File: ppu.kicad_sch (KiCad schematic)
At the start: 17 parts, among them U1 STM32U073CCUx, Y4 CM7V-T1A-32.768KHZ

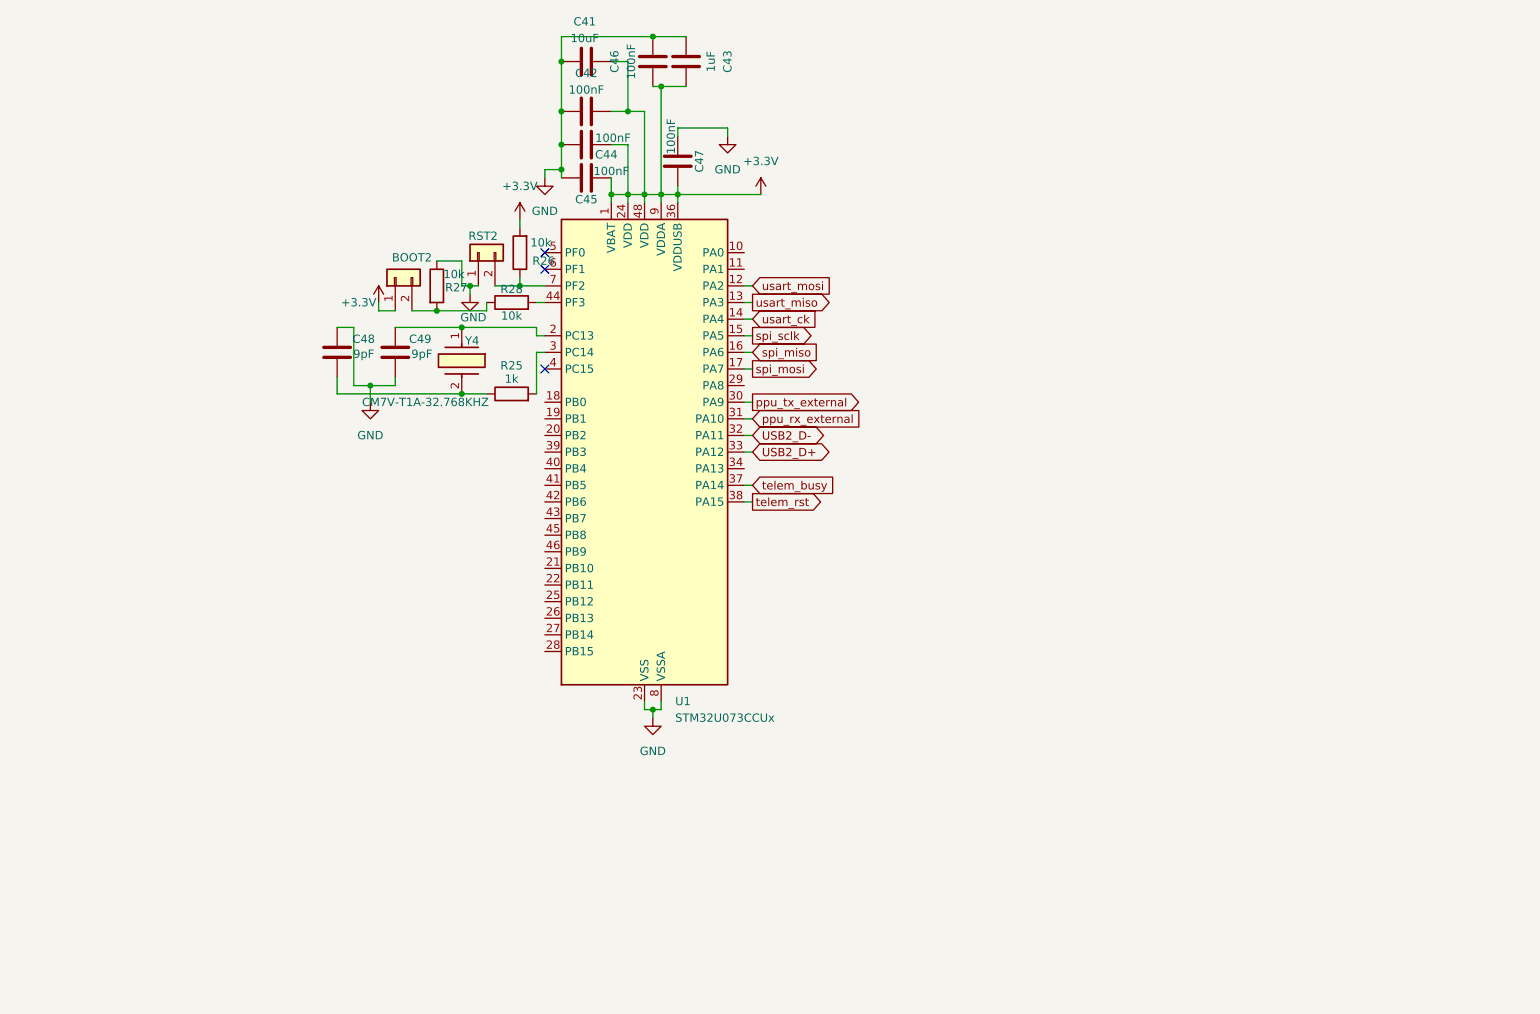
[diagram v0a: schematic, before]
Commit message: added in the flash chip and micro sd card, rerouted some stuff, looking real nice rn - still need to finish rf, pyros, and add in the piezo
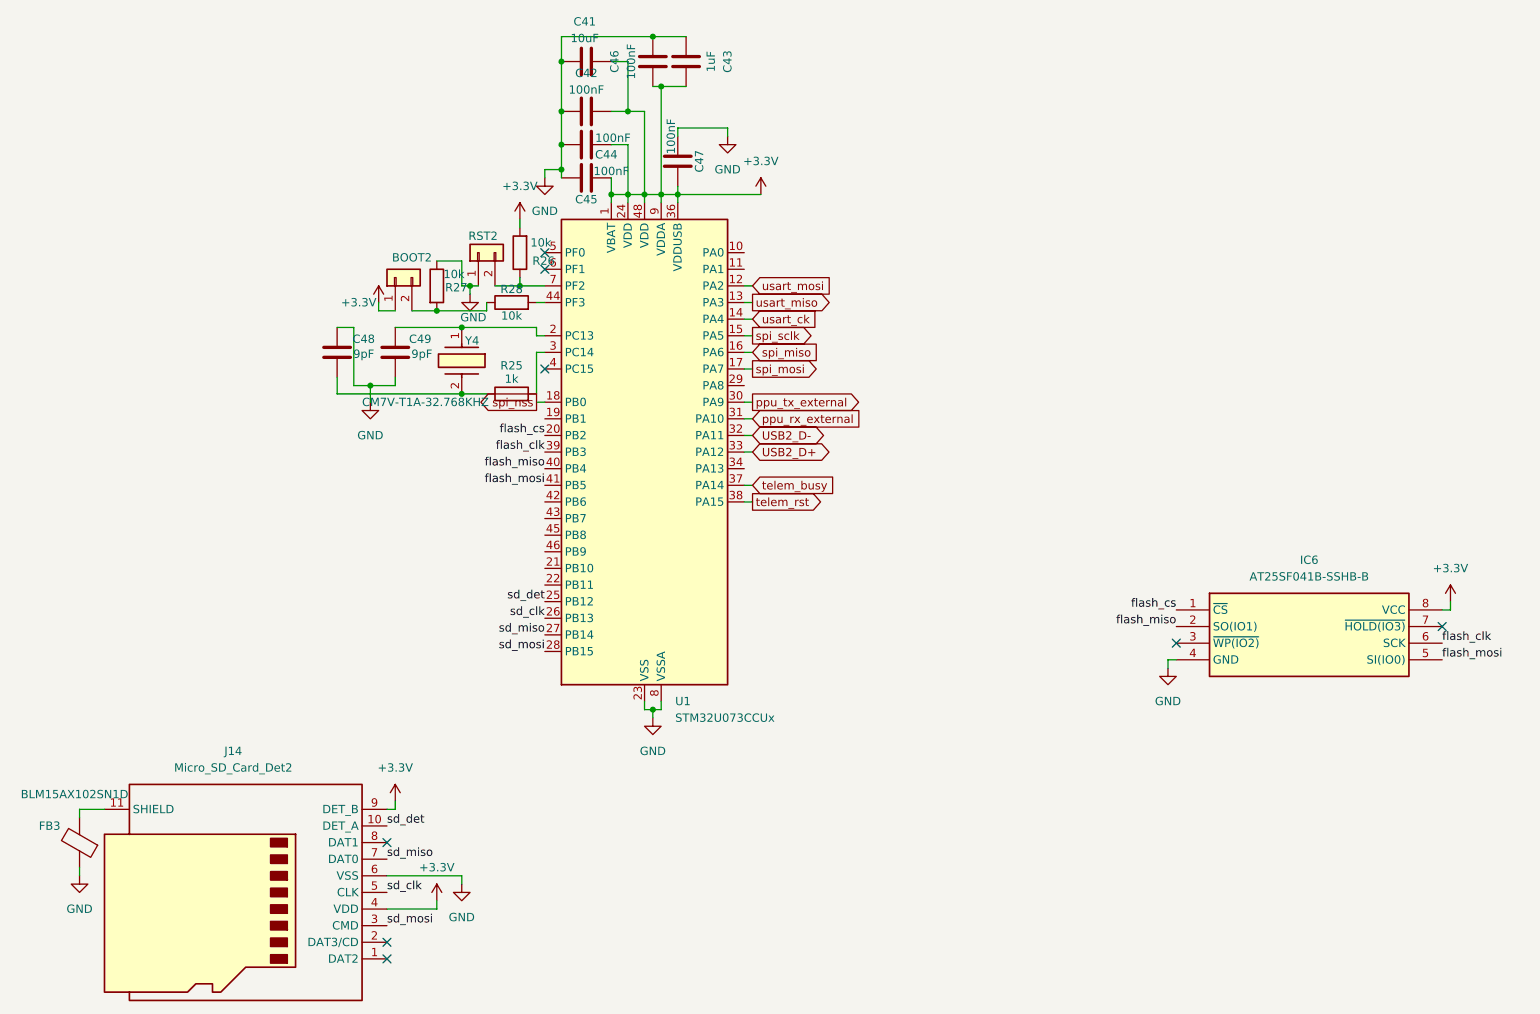
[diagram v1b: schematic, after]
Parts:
- added FB3: BLM15AX102SN1D, footprints:NFZ15SG152SN10B, symbol Device:FerriteBead
- added IC6: AT25SF041B-SSHB-B, footprints:SOIC127P600X175-8N, symbol AT25SF041B-SSHB-B:AT25SF041B-SSHB-B
- added J14: Micro_SD_Card_Det2, Connector_Card:microSD_HC_Molex_104031-0811, symbol Connector:Micro_SD_Card_Det2
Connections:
- net +3.3V: now also IC6.8 (VCC), J14.4 (VDD), J14.9 (DET_B)
- net GND: now also FB3.1, IC6.4 (GND), J14.6 (VSS)
- net spi_nss: now reaches U1.18 (PB0)
- net flash_cs: now reaches U1.20 (PB2)
- net flash_cs: now also IC6.1 (~{CS})
- net sd_det: now reaches U1.25 (PB12)
- net sd_det: now also J14.10 (DET_A)
- net sd_clk: now reaches U1.26 (PB13)
- net sd_clk: now also J14.5 (CLK)
- net sd_miso: now reaches U1.27 (PB14)
- net sd_miso: now also J14.7 (DAT0)
- net sd_mosi: now reaches U1.28 (PB15)
- net sd_mosi: now also J14.3 (CMD)
- net flash_clk: now reaches U1.39 (PB3)
- net flash_clk: now also IC6.6 (SCK)
- net flash_miso: now reaches U1.40 (PB4)
- net flash_miso: now also IC6.2 (SO(IO1))
- net flash_mosi: now reaches U1.41 (PB5)
- net flash_mosi: now also IC6.5 (SI(IO0))
- new net: FB3.2, J14.11 (SHIELD)
- no-connect marks 3 -> 8

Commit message: added piezo buzzer, rf hopefully finished! just need to send to mpk for check now
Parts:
- added LS1: PS1240P02BT, footprints:PS1240P02BT, symbol PS1240P02BT:PS1240P02BT
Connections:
- net GND: now also LS1.1
- net at U1.10 (PA0): now also LS1.2
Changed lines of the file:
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@@
+	(wire
+		(pts
+			(xy 142.24 83.82) (xy 142.24 82.55)
+		)
+		(stroke
+			(width 0)
+			(type default)
+		)
+	)
 	(wire
 		(pts
@@
 	(wire
 		(pts
+			(xy 127 80.01) (xy 143.51 80.01)
+		)
+		(stroke
+			(width 0)
+			(type default)
+		)
+	)
+	(wire
+		(pts
 			(xy 234.95 133.35) (xy 234.95 134.62)
 		)
@@
 		(pts
 			(xy 72.39 175.26) (xy 83.82 175.26)
+		)
+		(stroke
+			(width 0)
+			(type default)
+		)
+	)
+	(wire
+		(pts
+			(xy 142.24 82.55) (xy 143.51 82.55)
 		)
 		(stroke
@@
 	)
 	(symbol
+		(lib_id "PS1240P02BT:PS1240P02BT")
+		(at 143.51 80.01 0)
+		(unit 1)
+		(exclude_from_sim no)
+		(in_bom yes)
+		(on_board yes)
+		(dnp no)
+		(fields_autoplaced yes)
+		(property "Reference" "LS1"
+			(at 154.94 80.0099 0)
+			(effects
+				(font
+					(size 1.27 1.27)
+				)
+				(justify left)
+			)
+		)
+		(property "Value" "PS1240P02BT"
+			(at 154.94 82.5499 0)
+			(effects
+				(font
+					(size 1.27 1.27)
+				)
+				(justify left)
+			)
+		)
+		(property "Footprint" "footprints:PS1240P02BT"
+			(at 154.94 182.55 0)
+			(effects
+				(font
+					(size 1.27 1.27)
+				)
+				(justify left top)
+				(hide yes)
+			)
+		)
+		(property "Datasheet" "https://product.tdk.com/system/files/dam/doc/product/sw_piezo/sw_piezo/piezo-buzzer/catalog/piezoelectronic_buzzer_ps_en.pdf"
+			(at 154.94 282.55 0)
+			(effects
+				(font
+					(size 1.27 1.27)
+				)
+				(justify left top)
+				(hide yes)
+			)
+		)
+		(property "Description" "Piezoelectric Buzzers, Sound Pressure Level=70dB min, Freq.=4000Hz nom"
+			(at 143.51 80.01 0)
+			(effects
+				(font
+					(size 1.27 1.27)
+				)
+				(hide yes)
+			)
+		)
+		(property "Height" ""
+			(at 154.94 482.55 0)
+			(effects
+				(font
+					(size 1.27 1.27)
+				)
+				(justify left top)
+				(hide yes)
+			)
+		)
+		(property "Mouser Part Number" "810-PS1240P02BT"
+			(at 154.94 582.55 0)
+			(effects
+				(font
+					(size 1.27 1.27)
+				)
+				(justify left top)
+				(hide yes)
+			)
+		)
+		(property "Mouser Price/Stock" "https://www.mouser.co.uk/ProductDetail/TDK/PS1240P02BT?qs=d7g9p1yFhWaZXSY9MjKMkw%3D%3D"
+			(at 154.94 682.55 0)
+			(effects
+				(font
+					(size 1.27 1.27)
+				)
+				(justify left top)
+				(hide yes)
+			)
+		)
+		(property "Manufacturer_Name" "TDK"
+			(at 154.94 782.55 0)
+			(effects
+				(font
+					(size 1.27 1.27)
+				)
+				(justify left top)
+				(hide yes)
+			)
+		)
+		(property "Manufacturer_Part_Number" "PS1240P02BT"
+			(at 154.94 882.55 0)
+			(effects
+				(font
+					(size 1.27 1.27)
+				)
+				(justify left top)
+				(hide yes)
+			)
+		)
+		(pin "2"
+		)
+		(pin "1"
+		)
+		(instances
+			(project ""
+				(path "/d0cafa98-cc2a-4ab3-8dbc-f937bedf434b/1fd10c21-5691-4a3c-b52b-09de6b6b9389"
+					(reference "LS1")
+					(unit 1)
+				)
+			)
+		)
+	)
+	(symbol
 		(lib_id "Device:C")
 		(at 73.66 95.25 0)
@@
 					(unit 1)
 				)
+			)
+		)
+	)
+	(symbol
+		(lib_id "power:GND")
+		(at 142.24 83.82 0)
+		(unit 1)
+		(exclude_from_sim no)
+		(in_bom yes)
+		(on_board yes)
+		(dnp no)
+		(fields_autoplaced yes)
+		(property "Reference" "#PWR076"
+			(at 142.24 90.17 0)
+			(effects
+				(font
+					(size 1.27 1.27)
+				)
+				(hide yes)
+			)
+		)
+		(property "Value" "GND"
+			(at 142.24 88.9 0)
+			(effects
+				(font
+					(size 1.27 1.27)
+				)
+			)
+		)
+		(property "Footprint" ""
+			(at 142.24 83.82 0)
+			(effects
+				(font
+					(size 1.27 1.27)
+				)
+				(hide yes)
+			)
+		)
+		(property "Datasheet" ""
+			(at 142.24 83.82 0)
+			(effects
+				(font
+					(size 1.27 1.27)
+				)
+				(hide yes)
+			)
+		)
+		(property "Description" "Power symbol creates a global label with name \"GND\" , ground"
+			(at 142.24 83.82 0)
+			(effects
+				(font
+					(size 1.27 1.27)
+				)
+				(hide yes)
+			)
+		)
+		(pin "1"
+		)
+		(instances
+			(project ""
+				(path "/d0cafa98-cc2a-4ab3-8dbc-f937bedf434b/1fd10c21-5691-4a3c-b52b-09de6b6b9389"
+					(reference "#PWR076")
+					(unit 1)
+				)

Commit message: mosfet schematic done I hope
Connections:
- net cont_test_out: now reaches U1.11 (PA1)
- net c5_fire: now reaches U1.21 (PB10)
- net c6_fire: now reaches U1.22 (PB11)
- net arm: now reaches U1.29 (PA8)
- net c1_fire: now reaches U1.42 (PB6)
- net c2_fire: now reaches U1.43 (PB7)
- net c3_fire: now reaches U1.45 (PB8)
- net c4_fire: now reaches U1.46 (PB9)
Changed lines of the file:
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@@
+	(wire
+		(pts
+			(xy 95.25 130.81) (xy 96.52 130.81)
+		)
+		(stroke
+			(width 0)
+			(type default)
+		)
+	)
 	(wire
 		(pts
@@
 	(wire
 		(pts
+			(xy 95.25 125.73) (xy 96.52 125.73)
+		)
+		(stroke
+			(width 0)
+			(type default)
+		)
+	)
+	(wire
+		(pts
 			(xy 116.84 71.12) (xy 116.84 72.39)
 		)
@@
 	(wire
 		(pts
+			(xy 127 82.55) (xy 128.27 82.55)
+		)
+		(stroke
+			(width 0)
+			(type default)
+		)
+	)
+	(wire
+		(pts
 			(xy 127 87.63) (xy 128.27 87.63)
 		)
@@
 	(wire
 		(pts
+			(xy 95.25 123.19) (xy 96.52 123.19)
+		)
+		(stroke
+			(width 0)
+			(type default)
+		)
+	)
+	(wire
+		(pts
+			(xy 95.25 120.65) (xy 96.52 120.65)
+		)
+		(stroke
+			(width 0)
+			(type default)
+		)
+	)
+	(wire
+		(pts
+			(xy 95.25 128.27) (xy 96.52 128.27)
+		)
+		(stroke
+			(width 0)
+			(type default)
+		)
+	)
+	(wire
+		(pts
 			(xy 109.22 71.12) (xy 111.76 71.12)
 		)
@@
 	(wire
 		(pts
+			(xy 95.25 118.11) (xy 96.52 118.11)
+		)
+		(stroke
+			(width 0)
+			(type default)
+		)
+	)
+	(wire
+		(pts
 			(xy 96.52 67.31) (xy 96.52 68.58)
 		)
@@
 		(pts
 			(xy 114.3 149.86) (xy 113.03 149.86)
+		)
+		(stroke
+			(width 0)
+			(type default)
+		)
+	)
+	(wire
+		(pts
+			(xy 128.27 100.33) (xy 127 100.33)
 		)
 		(stroke
@@
 			)
 			(justify left bottom)
+		)
+	)
+	(global_label "c3_fire"
+		(shape output)
+		(at 95.25 123.19 180)
+		(fields_autoplaced yes)
+		(effects
+			(font
+				(size 1.27 1.27)
+			)
+			(justify right)
+		)
+		(property "Intersheetrefs" "${INTERSHEET_REFS}"
+			(at 85.7938 123.19 0)
+			(effects
+				(font
+					(size 1.27 1.27)
+				)
+				(justify right)
+				(hide yes)
+			)
 		)
 	)
@@
 		)
 	)
+	(global_label "cont_test_out"
+		(shape input)
+		(at 128.27 82.55 0)
+		(fields_autoplaced yes)
+		(effects
+			(font
+				(size 1.27 1.27)
+			)
+			(justify left)
+		)
+		(property "Intersheetrefs" "${INTERSHEET_REFS}"
+			(at 143.8945 82.55 0)
+			(effects
+				(font
+					(size 1.27 1.27)
+				)
+				(justify left)
+				(hide yes)
+			)
+		)
+	)
+	(global_label "c1_fire"
+		(shape output)
+		(at 95.25 118.11 180)
+		(fields_autoplaced yes)
+		(effects
+			(font
+				(size 1.27 1.27)
+			)
+			(justify right)
+		)
+		(property "Intersheetrefs" "${INTERSHEET_REFS}"
+			(at 85.7938 118.11 0)
+			(effects
+				(font
+					(size 1.27 1.27)
+				)
+				(justify right)
+				(hide yes)
+			)
+		)
+	)
 	(global_label "ppu_rx_external"
 		(shape input)
@@
 		)
 	)
+	(global_label "c2_fire"
+		(shape output)
+		(at 95.25 120.65 180)
+		(fields_autoplaced yes)
+		(effects
+			(font
+				(size 1.27 1.27)
+			)
+			(justify right)
+		)
+		(property "Intersheetrefs" "${INTERSHEET_REFS}"
+			(at 85.7938 120.65 0)
+			(effects
+				(font
+					(size 1.27 1.27)
+				)
+				(justify right)
+				(hide yes)
+			)
+		)
+	)
+	(global_label "c6_fire"
+		(shape output)
+		(at 95.25 130.81 180)
+		(fields_autoplaced yes)
+		(effects
+			(font
+				(size 1.27 1.27)
+			)
+			(justify right)
+		)
+		(property "Intersheetrefs" "${INTERSHEET_REFS}"
+			(at 85.7938 130.81 0)
+			(effects
+				(font
+					(size 1.27 1.27)
+				)
+				(justify right)
+				(hide yes)
+			)
+		)
+	)
 	(global_label "ppu_tx_external"
 		(shape output)
@@
 		)
 	)
+	(global_label "c4_fire"
+		(shape output)
+		(at 95.25 125.73 180)
+		(fields_autoplaced yes)
+		(effects
+			(font
+				(size 1.27 1.27)
+			)
+			(justify right)
+		)
+		(property "Intersheetrefs" "${INTERSHEET_REFS}"
+			(at 85.7938 125.73 0)
+			(effects
+				(font
+					(size 1.27 1.27)
+				)
+				(justify right)
+				(hide yes)
+			)
+		)
+	)
 	(global_label "spi_nss"
 		(shape output)
@@
 		)
 	)
+	(global_label "c5_fire"
+		(shape output)
+		(at 95.25 128.27 180)
+		(fields_autoplaced yes)
+		(effects
+			(font
+				(size 1.27 1.27)
+			)
+			(justify right)
+		)
+		(property "Intersheetrefs" "${INTERSHEET_REFS}"
+			(at 85.7938 128.27 0)
+			(effects
+				(font
+					(size 1.27 1.27)
+				)
+				(justify right)
+				(hide yes)
+			)
+		)
+	)
 	(global_label "spi_sclk"
 		(shape output)
@@
 			(effects
 				(font
+					(size 1.27 1.27)
+				)
+				(justify left)
+				(hide yes)
+			)
+		)
+	)
+	(global_label "arm"
+		(shape output)
+		(at 128.27 100.33 0)
+		(fields_autoplaced yes)
+		(effects
+			(font
+				(size 1.27 1.27)
+			)
+			(justify left)
+		)
+		(property "Intersheetrefs" "${INTERSHEET_REFS}"
+			(at 134.8837 100.33 0)
+			(effects
+				(font

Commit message: almost done routing! getting pretty close to done now
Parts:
- added Q6: MMBT2222A, Package_TO_SOT_SMD:SOT-23, symbol Transistor_BJT:MMBT2222A
- added R31: 1k, Resistor_SMD:R_0402_1005Metric, symbol Device:R
- U1: footprint Package_DFN_QFN:QFN-48-1EP_7x7mm_P0.5mm_EP5.6x5.6mm_ThermalVias -> Package_DFN_QFN:QFN-48-1EP_7x7mm_P0.5mm_EP5.6x5.6mm
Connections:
- net +3.3V: now also LS1.1
- net GND: now also Q6.3 (C); no longer LS1.1
- net at U1.10 (PA0): now also R31.1; no longer LS1.2
- new net: Q6.1 (B), R31.2
- new net: LS1.2, Q6.2 (E)
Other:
- moved on the sheet: LS1

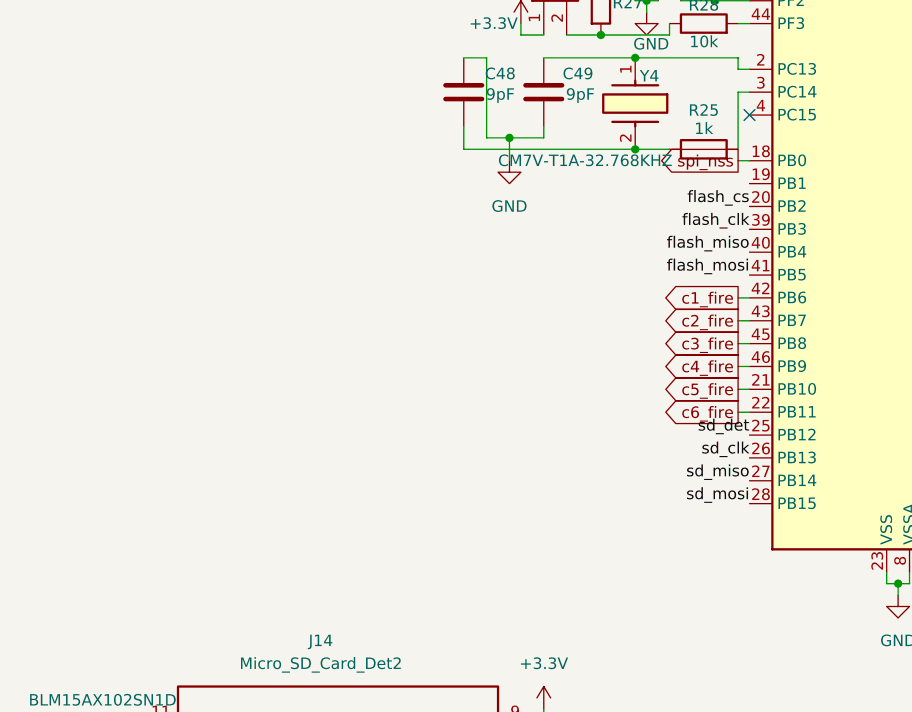
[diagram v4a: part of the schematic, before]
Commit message: finished the reroute - just need to redo silkscreen and verify everything
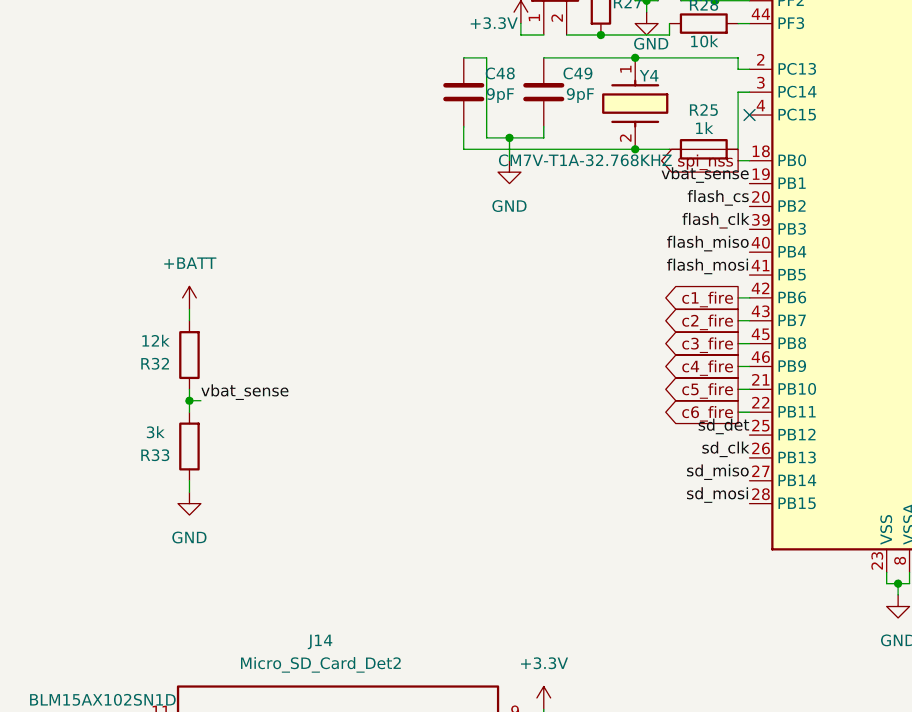
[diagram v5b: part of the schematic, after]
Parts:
- added R32: 12k, Resistor_SMD:R_0402_1005Metric, symbol Device:R
- added R33: 3k, Resistor_SMD:R_0402_1005Metric, symbol Device:R
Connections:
- net GND: now also R33.1
- net vbat_sense: now reaches U1.19 (PB1)
- net vbat_sense: now also R32.1, R33.2
- new net +BATT: R32.2
